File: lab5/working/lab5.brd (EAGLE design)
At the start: 132.5 x 132.5 mm, 53 parts, among them J1 ISP, Q1 FET, Q2 FET, Q3 FET, Q4 FET, U1 ATMEGA128RFA1, Y1 16MHz

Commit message: finished everything hopefully
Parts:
- moved C1 14.9 mm to (6.81, -5.30), turned to 0 degrees
- moved R5 14.0 mm to (-7.03, 2.00), turned to 180 degrees
- moved C3 13.3 mm to (-4.97, -22.9), turned to 135 degrees
- moved Y1 10.8 mm to (0.22, -4.82), turned to 180 degrees
- moved C16 9.97 mm to (13.8, -4.40), turned to 180 degrees
- moved C11 8.81 mm to (-20.9, 5.96), turned to 60 degrees
- moved B1 8.35 mm to (-13.8, -8.12)
- moved C8 7.90 mm to (-10.2, -10.3)
- moved C2 7.81 mm to (-6.90, -2.10), turned to 180 degrees
- moved R1 6.91 mm to (13.7, -11.6), turned to 180 degrees
- moved A1 6.65 mm to (-19.2, -13.4)
- moved C6 6.33 mm to (-12.3, -12.1)
- moved R4 5.51 mm to (-14.7, 7.64), turned to 330 degrees
- moved U$3 5.32 mm to (-22.4, -13.1)
- moved C12 5.19 mm to (6.83, -2.08), turned to 180 degrees
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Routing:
- net VBAT: track 0.00 -> 152.9 mm, vias 0 -> 1
- net 3.3V: track 0.00 -> 114.5 mm, vias 0 -> 4
- net RESET: track 0.00 -> 79.9 mm, vias 0 -> 1
- net N$12: track 0.00 -> 51.9 mm, vias 0 -> 1
- net TX1: track 0.00 -> 50.0 mm, vias 0 -> 1
- net RX1: track 0.00 -> 49.9 mm, vias 0 -> 2
- net N$16: track 0.00 -> 49.5 mm
- net PE3: track 0.00 -> 48.3 mm, vias 0 -> 2
- net PB5: track 0.00 -> 42.3 mm, vias 0 -> 2
- net GND: track 0.00 -> 39.2 mm, vias 0 -> 27
- net PE5: track 0.00 -> 39.2 mm, vias 0 -> 2
- net TX0: track 0.00 -> 38.3 mm
- net PE4: track 0.00 -> 35.6 mm
- net SCL: track 0.00 -> 25.2 mm, vias 0 -> 2
- net SDA: track 0.00 -> 23.2 mm, vias 0 -> 2
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
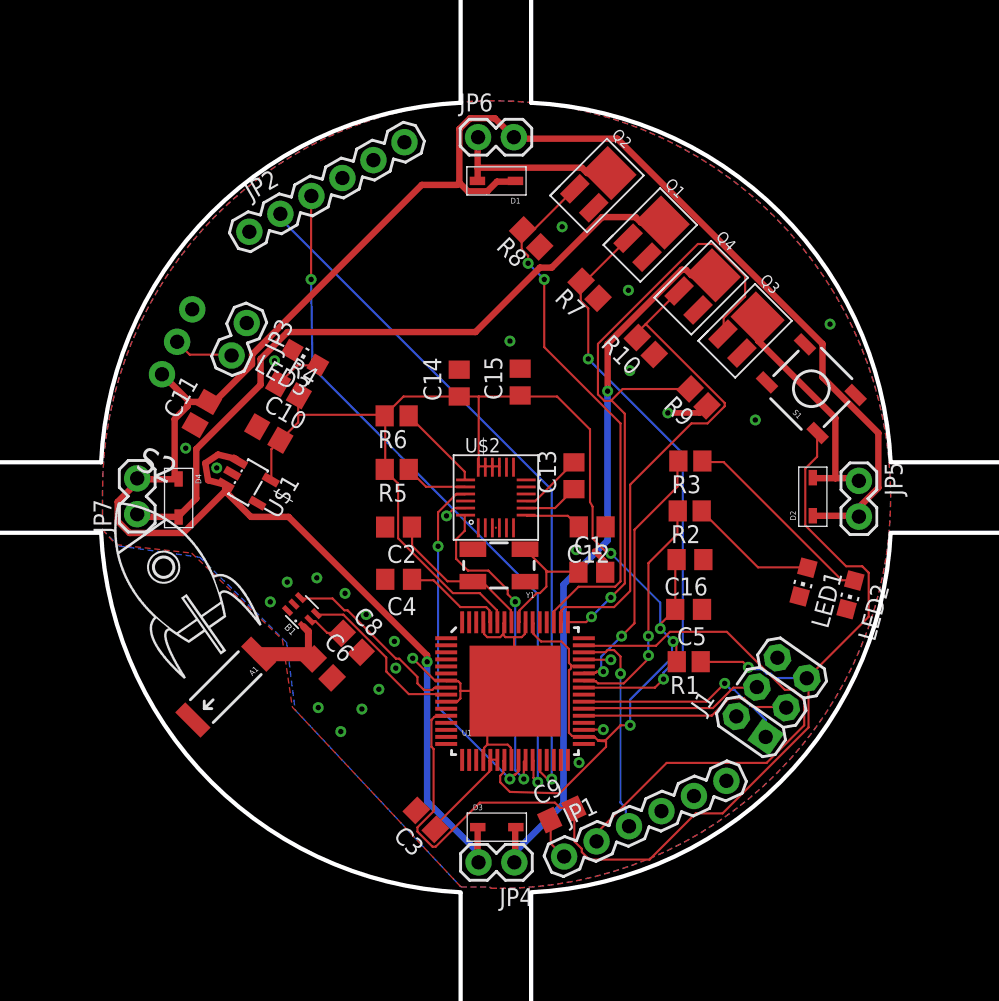
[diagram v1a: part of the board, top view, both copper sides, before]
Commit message: foxed clearance/ notation issues
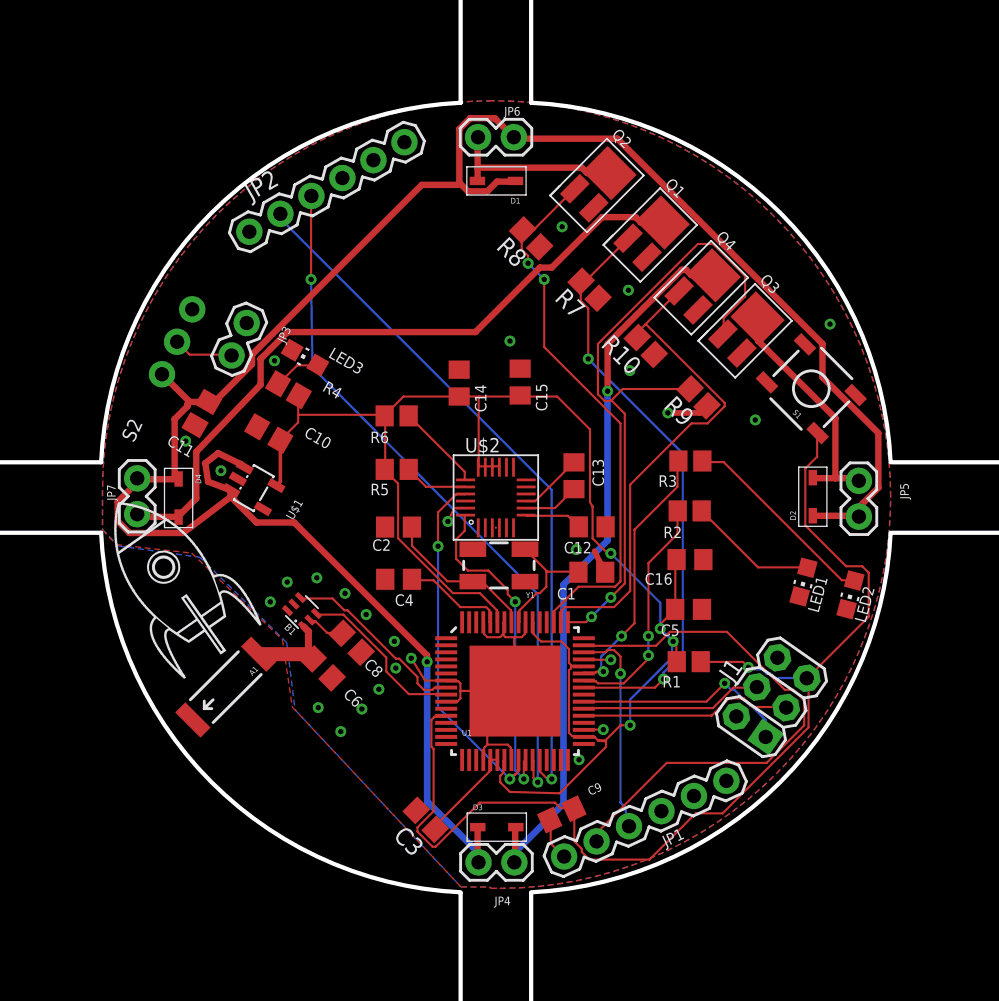
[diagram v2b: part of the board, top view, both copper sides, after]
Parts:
- moved U$1 0.57 mm to (-17.2, 0.67)
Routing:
- net VBAT: track 152.9 -> 153.6 mm
